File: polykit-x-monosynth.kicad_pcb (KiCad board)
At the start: 2 copper layers, 200 x 100 mm, 171 parts, among them J1 OUT LEFT, J10 PWM CV, J11 RES CV, J12 FREQ CV, J13 PITCH CV 1V/OCT, J14 EXT IN, J15 VCA CV, J16 HARD SYNC, J17 SOFT SYNC, J18 FM, J19 MULT, J2 OUT RIGHT, J20 WAVE IN, J21 ATT IN (+5V), J22 MULT1, J23 MULT2, J24 ATT OUT, J25 MIX IN2, J26 MIX IN1 (-5V), J27 MIX IN2, J28 WAVE OUT, J29 MIX OUT, J3 ADSR_OUT, J4 GATE, J5 TRIGGER, J6 Conn_01x36, J7 12V AC, J8 LFO, J9 PAN_CV, Q1 BC847, Q2 BC857, Q3 BC847, SW1 EXT_ON, SW2 FILTER_A, SW3 FILTER_B, SW4 FILTER_C, SW5 RES_MODE, SW6 FREQ_MODE, SW7 SAW_TRIANGLE, U1 MC78M12_TO252, U2 MC79M12_TO252, U3 L78L05_SO8, U4 L79L05_SO8, U5 TL074, U6 TL074, U7 TL074, U8 TL074, U9 TL072

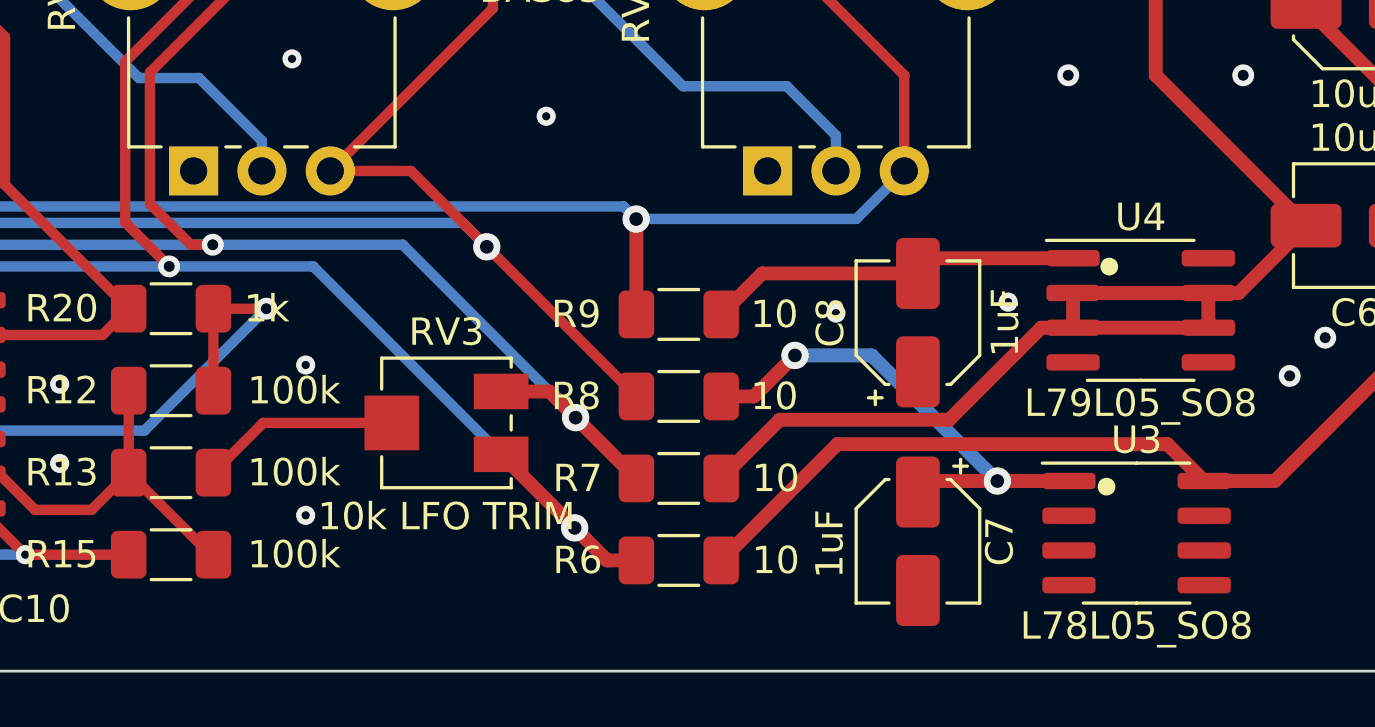
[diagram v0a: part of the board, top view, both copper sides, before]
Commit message: Fix power supply, add schematics pdf
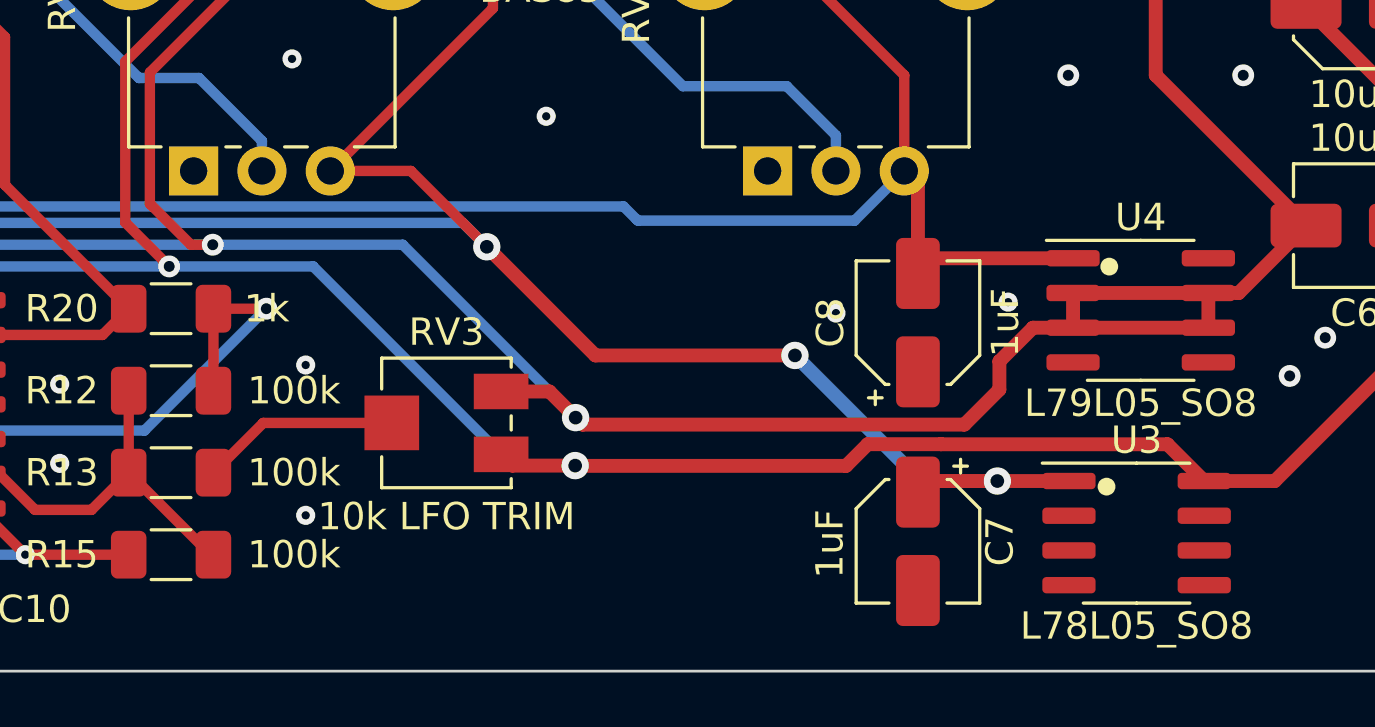
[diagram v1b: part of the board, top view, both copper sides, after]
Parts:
- removed R6, R7, R8, R9: 10, Resistor_SMD:R_1206_3216Metric_Pad1.30x1.75mm_HandSolder
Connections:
- C5 pad 1: Net-(C5-Pad1) -> +12V
- C6 pad 2: Net-(C6-Pad2) -> -12V
- C7 pad 1: Net-(C7-Pad1) -> +5V
- C8 pad 2: Net-(C8-Pad2) -> -5V
- U1 pad 3: Net-(C5-Pad1) -> +12V
- U2 pad 3: Net-(C6-Pad2) -> -12V
- U3 pad 1: Net-(C7-Pad1) -> +5V
- U3 pad 8: Net-(C5-Pad1) -> +12V
- U4 pad 1: Net-(C8-Pad2) -> -5V
- U4 pad 2: Net-(C6-Pad2) -> -12V
- U4 pad 3: Net-(C6-Pad2) -> -12V
- U4 pad 6: Net-(C6-Pad2) -> -12V
- U4 pad 7: Net-(C6-Pad2) -> -12V
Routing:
- net -12V: track 313.8 -> 385.5 mm
- net Net-(C6-Pad2): track 69.6 -> 0.00 mm
- net Net-(C5-Pad1): track 56.2 -> 0.00 mm
- net +12V: track 313.2 -> 368.7 mm
- net +5V: track 541.5 -> 561.7 mm, vias 5 -> 7
- net Net-(C7-Pad1): track 18.3 -> 0.00 mm, vias 2 -> 0
- net Net-(C8-Pad2): track 13.7 -> 0.00 mm
- net -5V: track 323.7 -> 330.1 mm, vias 3 -> 2
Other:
- board text added: "Polykit X1 v0.0.3 Jan Knipper 2022 github.com/polykit"
- board text removed: "Polykit X1 v0.0.2 Jan Knipper 2022 github.com/polykit"
